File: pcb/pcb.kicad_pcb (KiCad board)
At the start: 2 copper layers, 57 parts, among them J1 AMT0440007DB0000G, J10 Conn_02x10_Counter_Clockwise, J11 Conn_01x03, J12 Conn_01x02, J15 Conn_01x10, J16 Conn_01x10, J2 AMT0440007DB0000G, J3 AMT0440007DB0000G, J4 AMT0440007DB0000G, J5 Conn_01x03, J6 Conn_01x03, J7 Conn_01x03, J8 Conn_01x03, J9 Conn_01x03, Q1 IRF9Z34NPBF, Q2 IRF9Z34NPBF, Q3 IRF9Z34NPBF, Q4 IRF9Z34NPBF, Q5 IRF9Z34NPBF, U1 ACS711ELCTR-12AB-T, U2 ACS711ELCTR-12AB-T, U3 ACS711ELCTR-12AB-T, U4 ACS711ELCTR-12AB-T, U5 ACS711ELCTR-12AB-T, U6 TXS0102DCUR, U7 TXS0102DCUR, U8 TXS0102DCUR, U9 NCP718BSNADJT1G

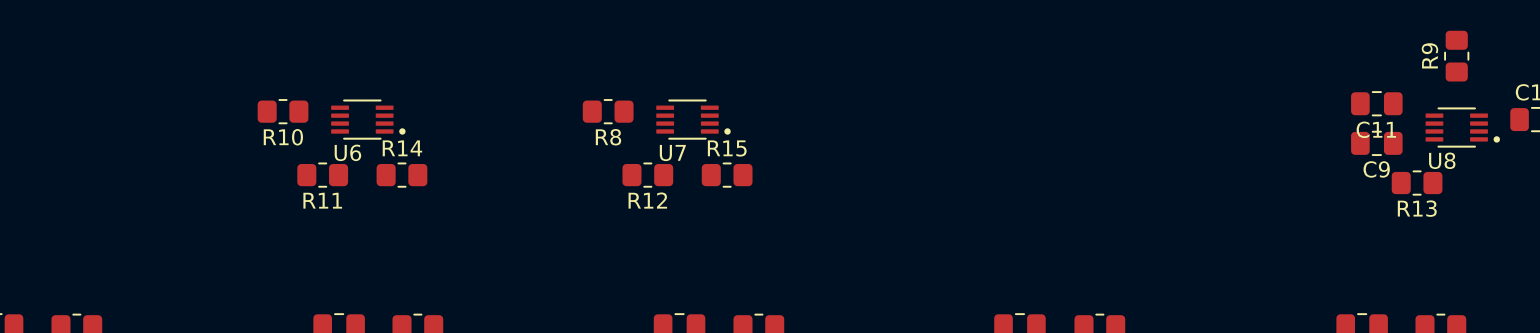
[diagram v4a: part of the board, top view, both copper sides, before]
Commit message: Swap servo label order for better layout
The schematic labels for the servo control and voltage signal nets were
previously assigned randomly. This commit reorders the labels so the two
larger servos are along the edge of the board for less interference on
adjacent Hall effect sensors. This commit also changes the labels so the
high side signals of each IC controls two MOSFETs that are close to each
other.
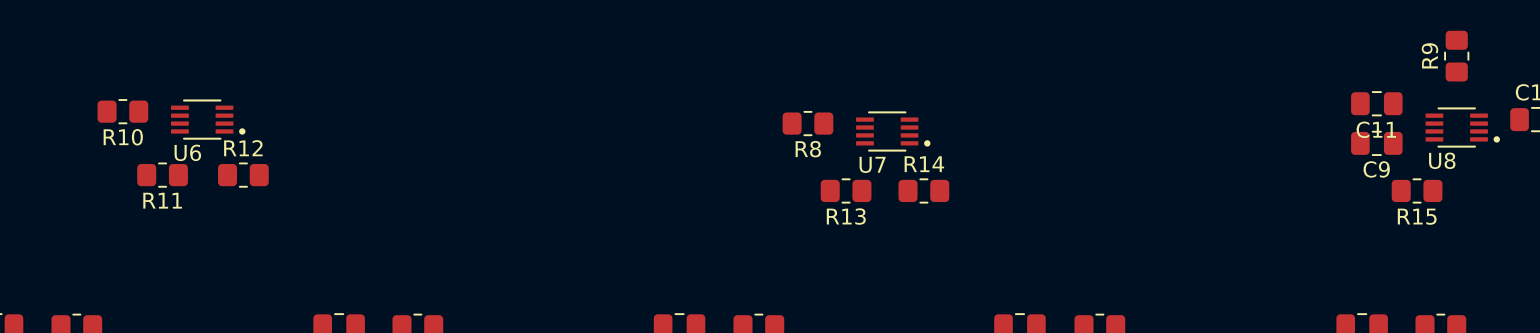
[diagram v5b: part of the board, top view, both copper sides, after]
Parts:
- moved R15 43.5 mm to (171.5, 85.0), turned to 180 degrees
- moved R13 36.0 mm to (135.5, 85.0)
- moved R14 32.9 mm to (140.4, 85.0)
- moved R12 25.5 mm to (97.5, 84.0), turned to 0 degrees
- moved R8 12.6 mm to (133.1, 80.8)
- moved U7 12.6 mm to (138.1, 81.2)
- moved R10 10.1 mm to (89.9, 80.0)
- moved R11 10.1 mm to (92.4, 84.0)
- moved U6 10.1 mm to (94.9, 80.5)
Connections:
- J10 pad 2: CTRL_SHOULDER -> CTRL_HAND
- J10 pad 5: CTRL_HAND -> CTRL_SHOULDER
- J6 pad 1: CTRL_SHOULDER -> CTRL_HAND
- J9 pad 1: CTRL_HAND -> CTRL_SHOULDER
- Q2 pad 1: SHUTOFF_SHOULDER_H -> SHUTOFF_HAND_H
- Q2 pad 3: +7V_SHOULDER -> +7V_HAND
- Q5 pad 1: SHUTOFF_HAND_H -> SHUTOFF_SHOULDER_H
- Q5 pad 3: +7V_HAND -> +7V_SHOULDER
- R12 pad 1: SHUTOFF_SHOULDER_H -> SHUTOFF_HAND_H
- R15 pad 1: SHUTOFF_HAND_H -> SHUTOFF_SHOULDER_H
- U2 pad 3: +7V_SHOULDER -> +7V_HAND
- U2 pad 4: +7V_SHOULDER -> +7V_HAND
- U2 pad 7: I_SENSE_SHOULDER -> I_SENSE_HAND
- U5 pad 3: +7V_HAND -> +7V_SHOULDER
- U5 pad 4: +7V_HAND -> +7V_SHOULDER
- U5 pad 7: I_SENSE_HAND -> I_SENSE_SHOULDER
- U6 pad 1: SHUTOFF_WRIST_H -> SHUTOFF_HAND_H
- U6 pad 4: SHUTOFF_WRIST_L -> SHUTOFF_HAND_L
- U7 pad 1: SHUTOFF_HAND_H -> SHUTOFF_WRIST_H
- U7 pad 4: SHUTOFF_HAND_L -> SHUTOFF_WRIST_L
- U7 pad 5: SHUTOFF_SHOULDER_L -> SHUTOFF_ELBOW_L
- U7 pad 8: SHUTOFF_SHOULDER_H -> SHUTOFF_ELBOW_H
- U8 pad 5: SHUTOFF_ELBOW_L -> SHUTOFF_SHOULDER_L
- U8 pad 8: SHUTOFF_ELBOW_H -> SHUTOFF_SHOULDER_H
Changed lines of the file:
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@@
 			(layers "*.Cu" "*.Mask")
 			(remove_unused_layers no)
-			(net "SHUTOFF_SHOULDER_H")
+			(net "SHUTOFF_HAND_H")
 			(pinfunction "G_1")
 			(pintype "input")
@@
 			(layers "*.Cu" "*.Mask")
 			(remove_unused_layers no)
-			(net "+7V_SHOULDER")
+			(net "+7V_HAND")
 			(pinfunction "S_3")
 			(pintype "passive")
@@
 			(layers "*.Cu" "*.Mask")
 			(remove_unused_layers no)
-			(net "CTRL_HAND")
+			(net "CTRL_SHOULDER")
 			(pinfunction "Pin_1_1")
 			(pintype "passive")
@@
 			(size 1.7526 0.6604)
 			(layers "F.Cu" "F.Mask" "F.Paste")
-			(net "+7V_SHOULDER")
+			(net "+7V_HAND")
 			(pinfunction "IP-_3")
 			(pintype "passive")
@@
 			(size 1.7526 0.6604)
 			(layers "F.Cu" "F.Mask" "F.Paste")
-			(net "+7V_SHOULDER")
+			(net "+7V_HAND")
 			(pinfunction "IP-_4")
 			(pintype "passive")
@@
 			(size 1.7526 0.6604)
 			(layers "F.Cu" "F.Mask" "F.Paste")
-			(net "I_SENSE_SHOULDER")
+			(net "I_SENSE_HAND")
 			(pinfunction "VIOUT_7")
 			(pintype "output")
@@
 			(layers "*.Cu" "*.Mask")
 			(remove_unused_layers no)
-			(net "SHUTOFF_HAND_H")
+			(net "SHUTOFF_SHOULDER_H")
 			(pinfunction "G_1")
 			(pintype "input")
@@
 			(layers "*.Cu" "*.Mask")
 			(remove_unused_layers no)
-			(net "+7V_HAND")
+			(net "+7V_SHOULDER")
 			(pinfunction "S_3")
 			(pintype "passive")
@@
 	(footprint "Resistor_SMD:R_0805_2012Metric_Pad1.20x1.40mm_HandSolder"
 		(layer "F.Cu")
-		(at 100 80 180)
+		(at 89.905 80 180)
 		(descr "Resistor SMD 0805 (2012 Metric), square (rectangular) end terminal, IPC-7351 nominal with elongated pad for handsoldering. (Body size source: IPC-SM-782 page 72, https://www.pcb-3d.com/wordpress/wp-content/uploads/ipc-sm-782a_amendment_1_and_2.pdf)")
 		(tags "resistor handsolder")
@@
 			(layers "*.Cu" "*.Mask")
 			(remove_unused_layers no)
-			(net "CTRL_SHOULDER")
+			(net "CTRL_HAND")
 			(pinfunction "Pin_2_2")
 			(pintype "passive")
@@
 			(layers "*.Cu" "*.Mask")
 			(remove_unused_layers no)
-			(net "CTRL_HAND")
+			(net "CTRL_SHOULDER")
 			(pinfunction "Pin_5_5")
 			(pintype "passive")
@@
 	(footprint "Resistor_SMD:R_0805_2012Metric_Pad1.20x1.40mm_HandSolder"
 		(layer "F.Cu")
-		(at 102.5 84 180)
+		(at 92.405 84 180)
 		(descr "Resistor SMD 0805 (2012 Metric), square (rectangular) end terminal, IPC-7351 nominal with elongated pad for handsoldering. (Body size source: IPC-SM-782 page 72, https://www.pcb-3d.com/wordpress/wp-content/uploads/ipc-sm-782a_amendment_1_and_2.pdf)")
 		(tags "resistor handsolder")
@@
 	(footprint "Resistor_SMD:R_0805_2012Metric_Pad1.20x1.40mm_HandSolder"
 		(layer "F.Cu")
-		(at 120.5 80 180)
+		(at 133.095 80.75 180)
 		(descr "Resistor SMD 0805 (2012 Metric), square (rectangular) end terminal, IPC-7351 nominal with elongated pad for handsoldering. (Body size source: IPC-SM-782 page 72, https://www.pcb-3d.com/wordpress/wp-content/uploads/ipc-sm-782a_amendment_1_and_2.pdf)")
 		(tags "resistor handsolder")
@@
 	(footprint "lib:SOP50P310X90-8N"
 		(layer "F.Cu")
-		(at 125.5 80.5 180)
+		(at 138.095 81.25 180)
 		(property "Reference" "U7"
 			(at 0.925 -2.135 0)
@@
 			(layers "F.Cu" "F.Mask" "F.Paste")
 			(roundrect_rratio 0.125)
-			(net "SHUTOFF_HAND_H")
+			(net "SHUTOFF_WRIST_H")
 			(pinfunction "B2_1")
 			(pintype "bidirectional")
@@
 			(layers "F.Cu" "F.Mask" "F.Paste")
 			(roundrect_rratio 0.125)
-			(net "SHUTOFF_HAND_L")
+			(net "SHUTOFF_WRIST_L")
 			(pinfunction "A2_4")
 			(pintype "bidirectional")
@@
 			(layers "F.Cu" "F.Mask" "F.Paste")
 			(roundrect_rratio 0.125)
-			(net "SHUTOFF_SHOULDER_L")
+			(net "SHUTOFF_ELBOW_L")
 			(pinfunction "A1_5")
 			(pintype "bidirectional")
@@
 			(layers "F.Cu" "F.Mask" "F.Paste")
 			(roundrect_rratio 0.125)
-			(net "SHUTOFF_SHOULDER_H")
+			(net "SHUTOFF_ELBOW_H")
 			(pinfunction "B1_8")
 			(pintype "bidirectional")
@@
 	(footprint "Resistor_SMD:R_0805_2012Metric_Pad1.20x1.40mm_HandSolder"
 		(layer "F.Cu")
-		(at 123 84 180)
+		(at 97.5 84)
 		(descr "Resistor SMD 0805 (2012 Metric), square (rectangular) end terminal, IPC-7351 nominal with elongated pad for handsoldering. (Body size source: IPC-SM-782 page 72, https://www.pcb-3d.com/wordpress/wp-content/uploads/ipc-sm-782a_amendment_1_and_2.pdf)")
 		(tags "resistor handsolder")
@@
 		(duplicate_pad_numbers_are_jumpers no)
 		(fp_line
-			(start -0.227064 0.735)
-			(end 0.227064 0.735)
+			(start -0.227064 -0.735)
+			(end 0.227064 -0.735)
 			(stroke
 				(width 0.12)
@@
 		)
 		(fp_line
-			(start -0.227064 -0.735)
-			(end 0.227064 -0.735)
+			(start -0.227064 0.735)
+			(end 0.227064 0.735)
 			(stroke
 				(width 0.12)
@@
 		)
 		(pad "1" smd roundrect
-			(at -1 0 180)
+			(at -1 0)
 			(size 1.2 1.4)
 			(layers "F.Cu" "F.Mask" "F.Paste")
 			(roundrect_rratio 0.208333)
-			(net "SHUTOFF_SHOULDER_H")
+			(net "SHUTOFF_HAND_H")
 			(pintype "passive")
 		)
 		(pad "2" smd roundrect
-			(at 1 0 180)
+			(at 1 0)
 			(size 1.2 1.4)
 			(layers "F.Cu" "F.Mask" "F.Paste")
@@
 			(layers "*.Cu" "*.Mask")
 			(remove_unused_layers no)
-			(net "CTRL_SHOULDER")
+			(net "CTRL_HAND")
 			(pinfunction "Pin_1_1")
 			(pintype "passive")
@@
 	(footprint "Resistor_SMD:R_0805_2012Metric_Pad1.20x1.40mm_HandSolder"
 		(layer "F.Cu")
-		(at 107.5 84)
+		(at 140.405 85)
 		(descr "Resistor SMD 0805 (2012 Metric), square (rectangular) end terminal, IPC-7351 nominal with elongated pad for handsoldering. (Body size source: IPC-SM-782 page 72, https://www.pcb-3d.com/wordpress/wp-content/uploads/ipc-sm-782a_amendment_1_and_2.pdf)")
 		(tags "resistor handsolder")
@@
 	(footprint "Resistor_SMD:R_0805_2012Metric_Pad1.20x1.40mm_HandSolder"
 		(layer "F.Cu")
-		(at 171.5 84.5 180)
+		(at 135.5 85 180)
 		(descr "Resistor SMD 0805 (2012 Metric), square (rectangular) end terminal, IPC-7351 nominal with elongated pad for handsoldering. (Body size source: IPC-SM-782 page 72, https://www.pcb-3d.com/wordpress/wp-content/uploads/ipc-sm-782a_amendment_1_and_2.pdf)")
 		(tags "resistor handsolder")
@@
 	(footprint "Resistor_SMD:R_0805_2012Metric_Pad1.20x1.40mm_HandSolder"
 		(layer "F.Cu")
-		(at 128 84)
+		(at 171.5 85 180)
 		(descr "Resistor SMD 0805 (2012 Metric), square (rectangular) end terminal, IPC-7351 nominal with elongated pad for handsoldering. (Body size source: IPC-SM-782 page 72, https://www.pcb-3d.com/wordpress/wp-content/uploads/ipc-sm-782a_amendment_1_and_2.pdf)")
 		(tags "resistor handsolder")
@@
 		(duplicate_pad_numbers_are_jumpers no)
 		(fp_line
-			(start -0.227064 -0.735)
-			(end 0.227064 -0.735)
+			(start -0.227064 0.735)
+			(end 0.227064 0.735)
 			(stroke
 				(width 0.12)
@@
 		)
 		(fp_line
-			(start -0.227064 0.735)
-			(end 0.227064 0.735)
+			(start -0.227064 -0.735)
+			(end 0.227064 -0.735)
 			(stroke
 				(width 0.12)
@@
 		)
 		(pad "1" smd roundrect
-			(at -1 0)
+			(at -1 0 180)
 			(size 1.2 1.4)
 			(layers "F.Cu" "F.Mask" "F.Paste")
 			(roundrect_rratio 0.208333)
-			(net "SHUTOFF_HAND_H")
+			(net "SHUTOFF_SHOULDER_H")
 			(pintype "passive")
 		)
 		(pad "2" smd roundrect
-			(at 1 0)
+			(at 1 0 180)
 			(size 1.2 1.4)
 			(layers "F.Cu" "F.Mask" "F.Paste")
@@
 	(footprint "lib:SOP50P310X90-8N"
 		(layer "F.Cu")
-		(at 105 80.5 180)
+		(at 94.905 80.5 180)
 		(property "Reference" "U6"
 			(at 0.925 -2.135 0)
@@
 			(layers "F.Cu" "F.Mask" "F.Paste")
 			(roundrect_rratio 0.125)
-			(net "SHUTOFF_WRIST_H")
+			(net "SHUTOFF_HAND_H")
 			(pinfunction "B2_1")
 			(pintype "bidirectional")
@@
 			(layers "F.Cu" "F.Mask" "F.Paste")
 			(roundrect_rratio 0.125)
-			(net "SHUTOFF_WRIST_L")
+			(net "SHUTOFF_HAND_L")
 			(pinfunction "A2_4")
 			(pintype "bidirectional")
@@
 			(size 1.7526 0.6604)
 			(layers "F.Cu" "F.Mask" "F.Paste")
-			(net "+7V_HAND")
+			(net "+7V_SHOULDER")
 			(pinfunction "IP-_3")
 			(pintype "passive")
@@
 			(size 1.7526 0.6604)
 			(layers "F.Cu" "F.Mask" "F.Paste")
-			(net "+7V_HAND")
+			(net "+7V_SHOULDER")
 			(pinfunction "IP-_4")
 			(pintype "passive")
@@
 			(size 1.7526 0.6604)
 			(layers "F.Cu" "F.Mask" "F.Paste")
-			(net "I_SENSE_HAND")
+			(net "I_SENSE_SHOULDER")
 			(pinfunction "VIOUT_7")
 			(pintype "output")
@@
 			(layers "F.Cu" "F.Mask" "F.Paste")
 			(roundrect_rratio 0.125)
-			(net "SHUTOFF_ELBOW_L")
+			(net "SHUTOFF_SHOULDER_L")
 			(pinfunction "A1_5")
 			(pintype "bidirectional")
@@
 			(layers "F.Cu" "F.Mask" "F.Paste")
 			(roundrect_rratio 0.125)
-			(net "SHUTOFF_ELBOW_H")
+			(net "SHUTOFF_SHOULDER_H")
 			(pinfunction "B1_8")
 			(pintype "bidirectional")

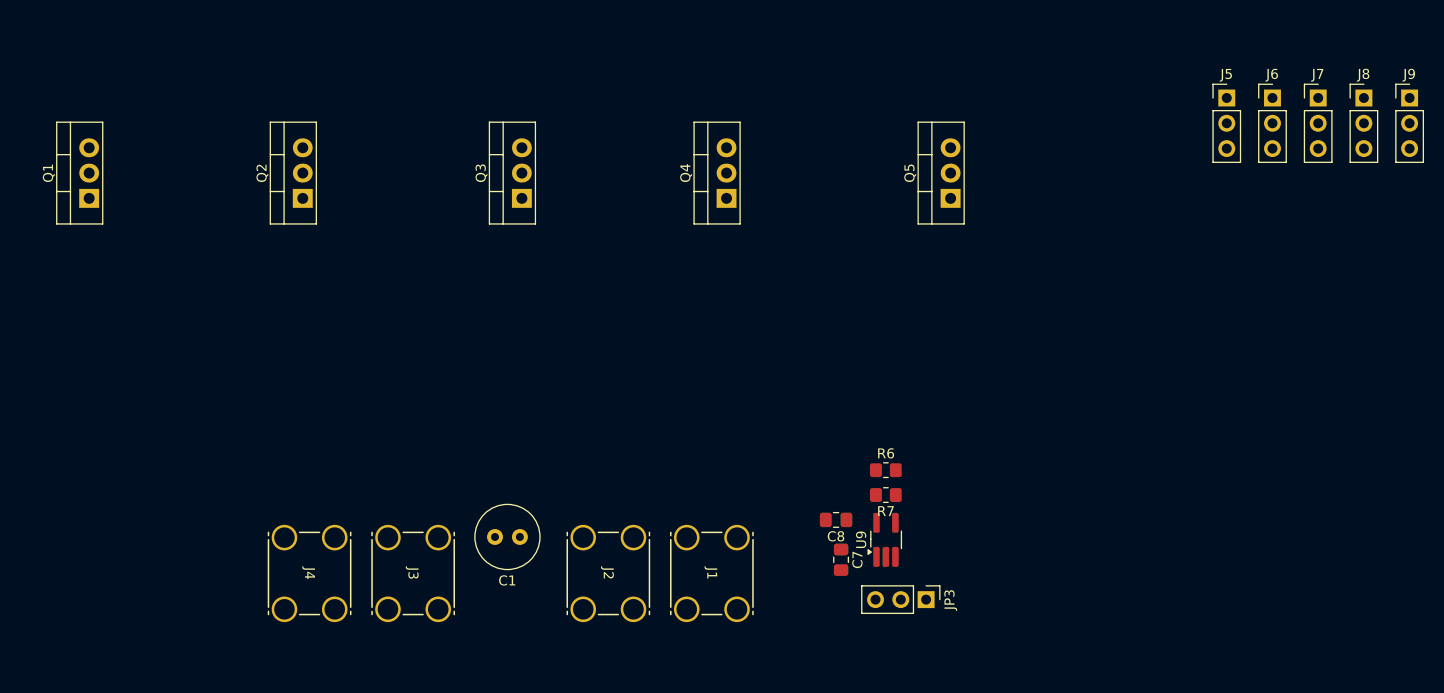
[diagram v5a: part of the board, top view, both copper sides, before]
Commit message: Move +7V terminals and servo power components
The previous layout of the +7V screw terminals, PMOSFETS, servo headers,
and +5V power supply didn't take into account how the Hall effect sensor
power planes were going to be routed. This commit moves these components
and subcircuits to make the power planes easier to route.
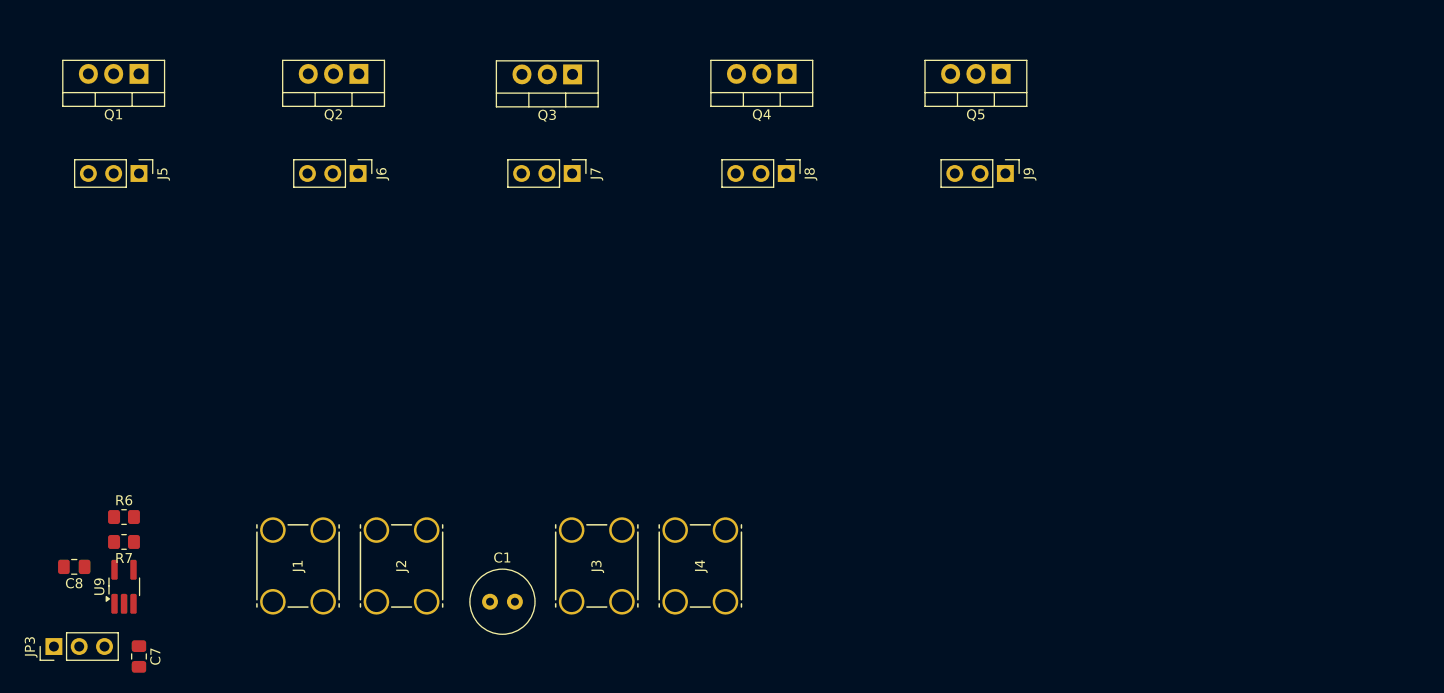
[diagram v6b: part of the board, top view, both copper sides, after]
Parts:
- moved J5 109.5 mm to (92.0, 134.5), turned to -90 degrees
- moved J6 92.1 mm to (114.0, 134.5), turned to -90 degrees
- moved JP3 87.7 mm to (83.5, 182.0), turned to 90 degrees
- moved C8 76.6 mm to (85.5, 174.0)
- moved R6 76.6 mm to (90.5, 169.0)
- moved R7 76.6 mm to (90.5, 171.5)
- moved U9 76.6 mm to (90.5, 176.0)
- moved J7 75.3 mm to (135.5, 134.5), turned to -90 degrees
- moved C7 71.2 mm to (92.0, 183.0)
- moved J8 58.5 mm to (157.0, 134.5), turned to -90 degrees
- moved J1 47.1 mm to (105.4, 177.5), turned to 90 degrees
- moved J9 41.3 mm to (179.0, 134.5), turned to -90 degrees
- moved J4 34.8 mm to (145.8, 177.5), turned to 90 degrees
- moved J2 26.6 mm to (115.8, 177.5), turned to 90 degrees
- moved J3 14.9 mm to (135.4, 177.5), turned to 90 degrees
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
